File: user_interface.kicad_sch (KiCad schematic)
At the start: 0 parts

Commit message: feat: populate sensor and user interface schematic sheets; assign footprints
- Populated the Sensors schematic sheet with the following components:
    - BME280: Temperature and humidity sensor
    - Photoresistor: For measuring ambient light levels
    - Sound Sensor Section: Includes a microphone and preamplifier to amplify audio signals for microcontroller processing

- Populated the User Interface schematic sheet with:
    - Boot and reset controls for the microcontroller
    - Breakout lines for external devices:
        - One for I²C-based peripherals (e.g., OLED display)
        - One for general-purpose I/O devices

- Both the Sensors and User Interface sheets access necessary pins (e.g., I²C, GPIO, control signals) from the parent ESP32
sheet using hierarchical labels, enabling clean and modular design.

- Assigned appropriate footprints to all components.
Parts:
- added C19, C20: 0u1, Capacitor_SMD:C_0805_2012Metric, symbol Device:C
- added J4: Conn_01x04_Pin, Connector_PinHeader_2.54mm:PinHeader_1x04_P2.54mm_Vertical, symbol Connector:Conn_01x04_Pin
- added J5: Conn_01x05_Pin, Connector_PinHeader_2.54mm:PinHeader_1x05_P2.54mm_Vertical, symbol Connector:Conn_01x05_Pin
- added Q2, Q3: BC817, Package_TO_SOT_SMD:SOT-23, symbol Transistor_BJT:BC817
- added R30, R31, R32: 10k, Resistor_SMD:R_0805_2012Metric, symbol Device:R
- added S1: Boot, USLPT2819DT2TR:SW_USLPT2819DT2TR, symbol USLPT2819DT2TR:USLPT2819DT2TR
- added S2: Reset, USLPT2819DT2TR:SW_USLPT2819DT2TR, symbol USLPT2819DT2TR:USLPT2819DT2TR
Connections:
- new net: Q3.1 (B), R31.2
- new net: Q2.1 (B), R30.2
- new net +3.3V: J4.1 (Pin_1), J5.1 (Pin_1), R32.1
- new net BOOT: C19.2, Q2.2 (E), S1.3, S1.4
- new net DTR: Q2.3 (C), R31.1
- new net EN: C20.2, Q3.3 (C), R32.2, S2.3, S2.4
- new net GND: C19.1, C20.1, J4.4 (Pin_4), J5.5 (Pin_5), S1.1, S1.2, S2.1, S2.2
- new net GPIO18: J5.3 (Pin_3)
- new net GPIO19: J5.4 (Pin_4)
- new net GPIO8: J5.2 (Pin_2)
- new net RTS: Q3.2 (E), R30.1
- new net SCL: J4.3 (Pin_3)
- new net SDA: J4.2 (Pin_2)
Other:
- note added: "Breakout for remaining pins"
- note added: "OLED display connector (I2C)"
- note added: "Reset and BOOT Buttons"

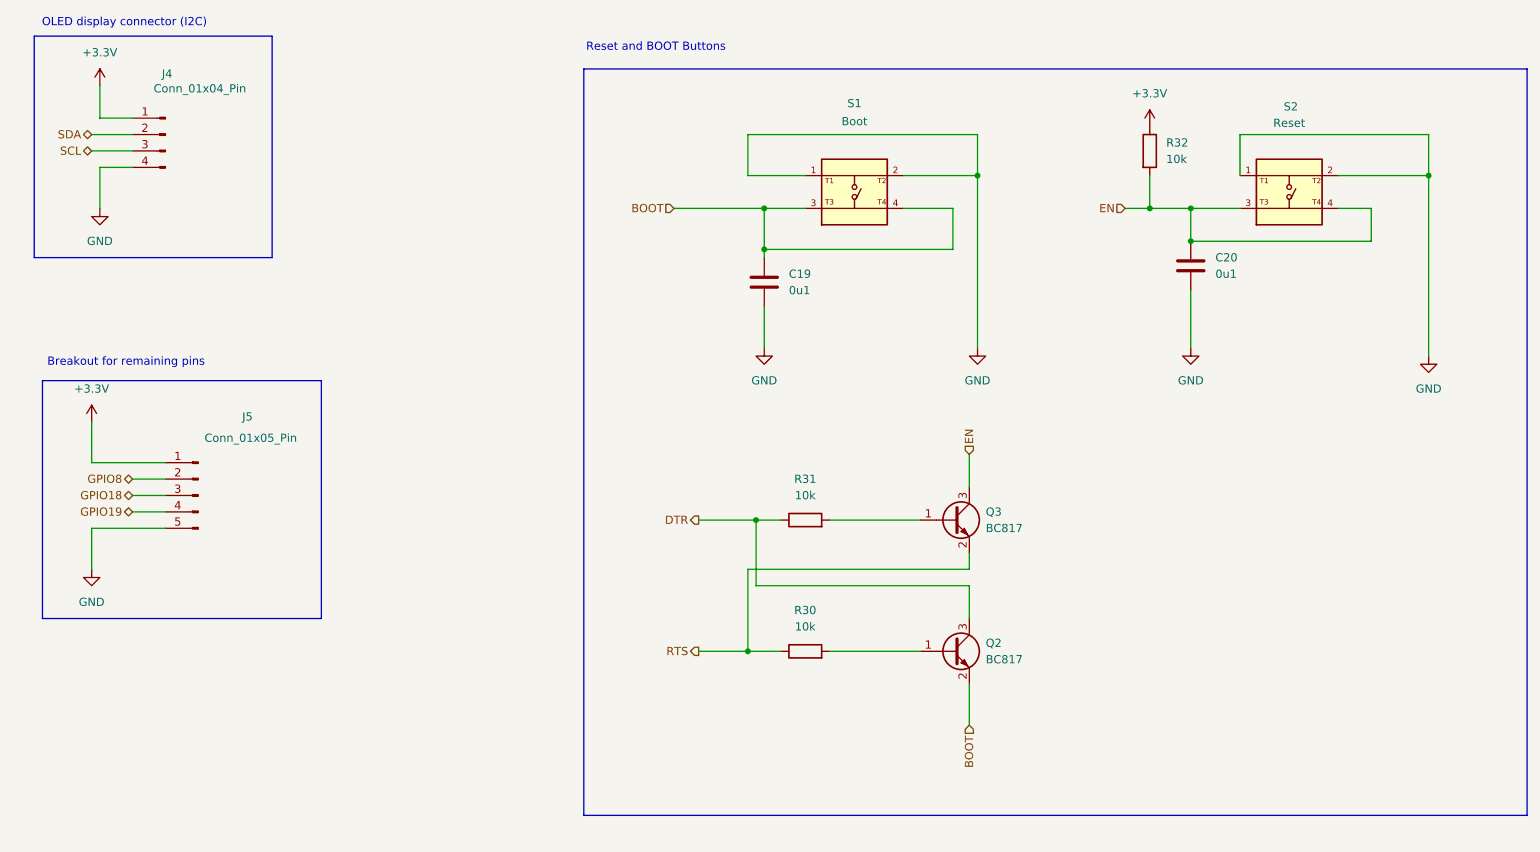
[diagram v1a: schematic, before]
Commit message: refactor: update label naming for net class scope resolution; set up PCB constraints
- Renamed schematic labels to follow a net class–based naming convention for
better scope resolution (e.g., labels in the SPI net class now use a SPI_ prefix).

- Configured the PCB stack-up to use a 4-layer board.

- Applied design constraints (e.g., trace width, spacing) based on the
PCB manufacturer's recommended specifications.
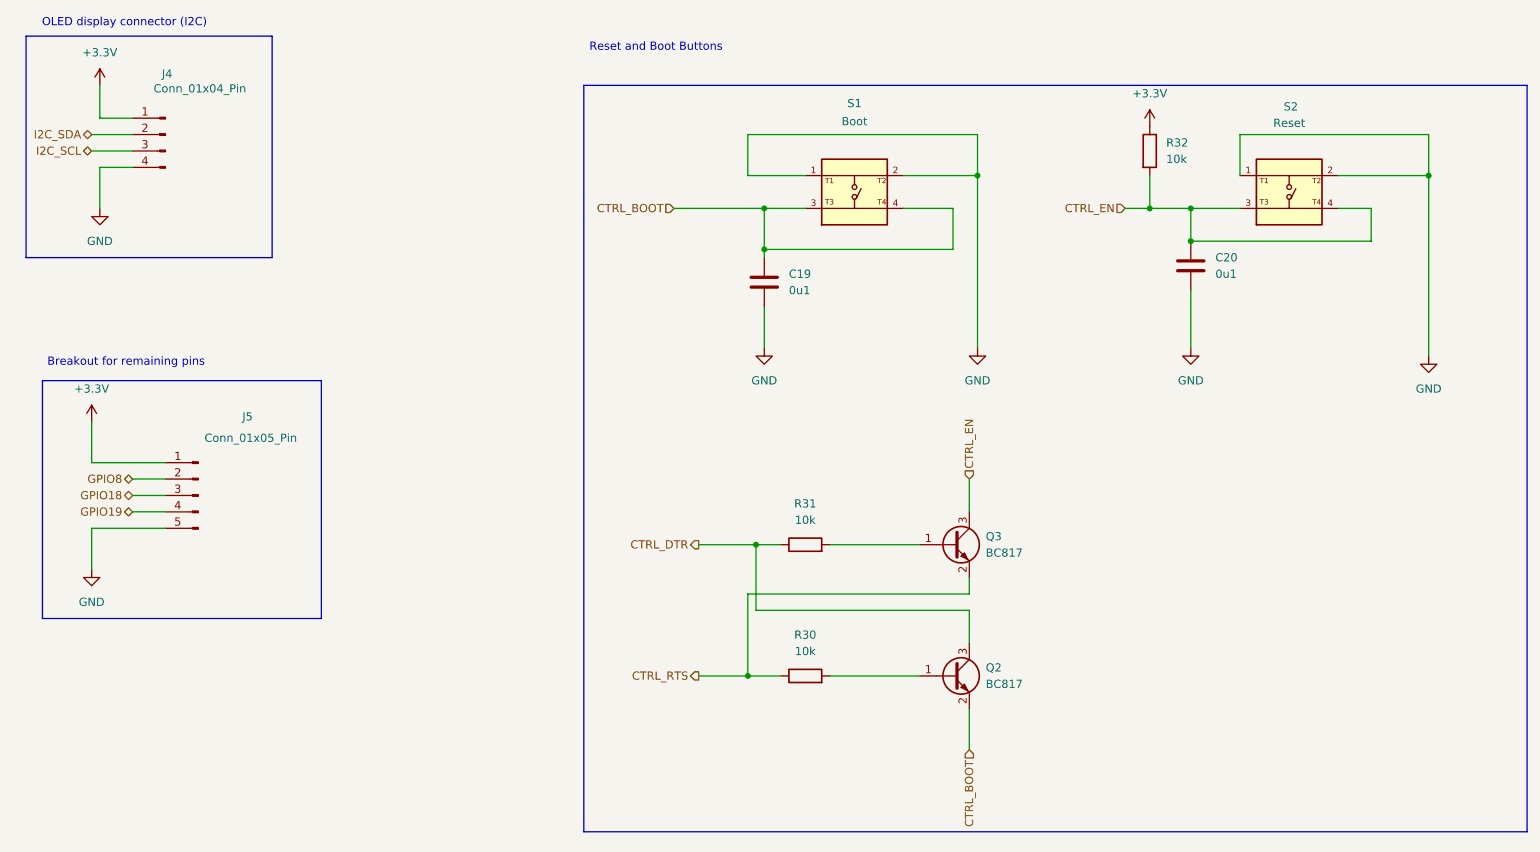
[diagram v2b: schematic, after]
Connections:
- net BOOT renamed CTRL_BOOT
- net DTR renamed CTRL_DTR
- net EN renamed CTRL_EN
- net RTS renamed CTRL_RTS
- net SCL renamed I2C_SCL
- net SDA renamed I2C_SDA
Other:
- note added: "Reset and Boot Buttons"
- note removed: "Reset and BOOT Buttons"
- moved on the sheet: Q2, Q3, R30, R31
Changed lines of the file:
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@@
 	)
 	(rectangle
-		(start 129.54 45.72)
-		(end 275.59 161.29)
+		(start 129.54 48.26)
+		(end 275.59 163.83)
 		(stroke
 			(width 0)
@@
 	)
 	(rectangle
-		(start 44.45 40.64)
+		(start 43.18 40.64)
 		(end 81.28 74.93)
 		(stroke
@@
 		)
 	)
-	(text "Reset and BOOT Buttons\n"
+	(text "Reset and Boot Buttons\n"
 		(exclude_from_sim no)
 		(at 140.716 42.418 0)
@@
 	)
 	(junction
-		(at 154.94 135.89)
+		(at 154.94 139.7)
 		(diameter 0)
 		(color 0 0 0 0)
@@
 	)
 	(junction
-		(at 156.21 115.57)
+		(at 156.21 119.38)
 		(diameter 0)
 		(color 0 0 0 0)
@@
 	(wire
 		(pts
-			(xy 154.94 123.19) (xy 154.94 135.89)
-		)
-		(stroke
-			(width 0)
-			(type default)
-		)
-	)
-	(wire
-		(pts
-			(xy 156.21 125.73) (xy 156.21 115.57)
-		)
-		(stroke
-			(width 0)
-			(type default)
-		)
-	)
-	(wire
-		(pts
-			(xy 189.23 120.65) (xy 189.23 123.19)
-		)
-		(stroke
-			(width 0)
-			(type default)
-		)
-	)
-	(wire
-		(pts
-			(xy 189.23 130.81) (xy 189.23 125.73)
+			(xy 154.94 127) (xy 154.94 139.7)
+		)
+		(stroke
+			(width 0)
+			(type default)
+		)
+	)
+	(wire
+		(pts
+			(xy 156.21 129.54) (xy 156.21 119.38)
+		)
+		(stroke
+			(width 0)
+			(type default)
+		)
+	)
+	(wire
+		(pts
+			(xy 189.23 124.46) (xy 189.23 127)
+		)
+		(stroke
+			(width 0)
+			(type default)
+		)
+	)
+	(wire
+		(pts
+			(xy 189.23 134.62) (xy 189.23 129.54)
 		)
 		(stroke
@@
 	(wire
 		(pts
-			(xy 189.23 123.19) (xy 154.94 123.19)
-		)
-		(stroke
-			(width 0)
-			(type default)
-		)
-	)
-	(wire
-		(pts
-			(xy 156.21 115.57) (xy 160.02 115.57)
+			(xy 189.23 127) (xy 154.94 127)
+		)
+		(stroke
+			(width 0)
+			(type default)
+		)
+	)
+	(wire
+		(pts
+			(xy 156.21 119.38) (xy 160.02 119.38)
 		)
 		(stroke
@@
 	(wire
 		(pts
-			(xy 189.23 140.97) (xy 189.23 147.32)
-		)
-		(stroke
-			(width 0)
-			(type default)
-		)
-	)
-	(wire
-		(pts
-			(xy 189.23 125.73) (xy 156.21 125.73)
-		)
-		(stroke
-			(width 0)
-			(type default)
-		)
-	)
-	(wire
-		(pts
-			(xy 154.94 135.89) (xy 160.02 135.89)
-		)
-		(stroke
-			(width 0)
-			(type default)
-		)
-	)
-	(wire
-		(pts
-			(xy 167.64 135.89) (xy 181.61 135.89)
+			(xy 189.23 144.78) (xy 189.23 151.13)
+		)
+		(stroke
+			(width 0)
+			(type default)
+		)
+	)
+	(wire
+		(pts
+			(xy 189.23 129.54) (xy 156.21 129.54)
+		)
+		(stroke
+			(width 0)
+			(type default)
+		)
+	)
+	(wire
+		(pts
+			(xy 154.94 139.7) (xy 160.02 139.7)
+		)
+		(stroke
+			(width 0)
+			(type default)
+		)
+	)
+	(wire
+		(pts
+			(xy 167.64 139.7) (xy 181.61 139.7)
 		)
 		(stroke
@@
 	(wire
 		(pts
-			(xy 189.23 105.41) (xy 189.23 110.49)
-		)
-		(stroke
-			(width 0)
-			(type default)
-		)
-	)
-	(wire
-		(pts
-			(xy 167.64 115.57) (xy 181.61 115.57)
+			(xy 189.23 109.22) (xy 189.23 114.3)
+		)
+		(stroke
+			(width 0)
+			(type default)
+		)
+	)
+	(wire
+		(pts
+			(xy 167.64 119.38) (xy 181.61 119.38)
 		)
 		(stroke
@@
 	(wire
 		(pts
-			(xy 147.32 135.89) (xy 154.94 135.89)
+			(xy 147.32 139.7) (xy 154.94 139.7)
 		)
 		(stroke
@@
 	(wire
 		(pts
-			(xy 147.32 115.57) (xy 156.21 115.57)
+			(xy 147.32 119.38) (xy 156.21 119.38)
 		)
 		(stroke
@@
 		)
 	)
-	(hierarchical_label "EN"
+	(hierarchical_label "CTRL_EN"
 		(shape input)
-		(at 189.23 105.41 90)
+		(at 189.23 109.22 90)
 		(effects
 			(font
@@
 		)
 	)
-	(hierarchical_label "SDA"
+	(hierarchical_label "I2C_SDA"
 		(shape bidirectional)
 		(at 53.34 55.88 180)
@@
 		)
 	)
-	(hierarchical_label "SCL"
+	(hierarchical_label "I2C_SCL"
 		(shape bidirectional)
 		(at 53.34 58.42 180)
@@
 		)
 	)
-	(hierarchical_label "EN"
+	(hierarchical_label "CTRL_EN"
 		(shape input)
 		(at 213.36 67.31 180)
@@
 		)
 	)
-	(hierarchical_label "DTR"
+	(hierarchical_label "CTRL_DTR"
 		(shape output)
-		(at 147.32 115.57 180)
+		(at 147.32 119.38 180)
 		(effects
 			(font
@@
 		)
 	)
-	(hierarchical_label "BOOT"
+	(hierarchical_label "CTRL_BOOT"
 		(shape input)
 		(at 143.51 67.31 180)
@@
 		)
 	)
-	(hierarchical_label "BOOT"
+	(hierarchical_label "CTRL_BOOT"
 		(shape input)
-		(at 189.23 147.32 270)
+		(at 189.23 151.13 270)
 		(effects
 			(font
@@
 		)
 	)
-	(hierarchical_label "RTS"
+	(hierarchical_label "CTRL_RTS"
 		(shape output)
-		(at 147.32 135.89 180)
+		(at 147.32 139.7 180)
 		(effects
 			(font
@@
 	(symbol
 		(lib_id "Device:R")
-		(at 163.83 115.57 90)
+		(at 163.83 119.38 90)
 		(unit 1)
 		(exclude_from_sim no)
@@
 		(fields_autoplaced yes)
 		(property "Reference" "R31"
-			(at 163.83 109.22 90)
+			(at 163.83 113.03 90)
 			(effects
 				(font
@@
 		)
 		(property "Value" "10k"
-			(at 163.83 111.76 90)
+			(at 163.83 115.57 90)
 			(effects
 				(font
@@
 		)
 		(property "Footprint" "Resistor_SMD:R_0805_2012Metric"
-			(at 163.83 117.348 90)
+			(at 163.83 121.158 90)
 			(effects
 				(font
@@
 		)
 		(property "Datasheet" "~"
-			(at 163.83 115.57 0)
+			(at 163.83 119.38 0)
 			(effects
 				(font
@@
 		)
 		(property "Description" "Resistor"
-			(at 163.83 115.57 0)
+			(at 163.83 119.38 0)
 			(effects
 				(font
@@
 	(symbol
 		(lib_id "Transistor_BJT:BC817")
-		(at 186.69 135.89 0)
+		(at 186.69 139.7 0)
 		(unit 1)
 		(exclude_from_sim no)
@@
 		(fields_autoplaced yes)
 		(property "Reference" "Q2"
-			(at 191.77 134.6199 0)
+			(at 191.77 138.4299 0)
 			(effects
 				(font
@@
 		)
 		(property "Value" "BC817"
-			(at 191.77 137.1599 0)
+			(at 191.77 140.9699 0)
 			(effects
 				(font
@@
 		)
 		(property "Footprint" "Package_TO_SOT_SMD:SOT-23"
-			(at 191.77 137.795 0)
+			(at 191.77 141.605 0)
 			(effects
 				(font
@@
 		)
 		(property "Datasheet" "https://www.onsemi.com/pub/Collateral/BC818-D.pdf"
-			(at 186.69 135.89 0)
+			(at 186.69 139.7 0)
 			(effects
 				(font
@@
 		)
 		(property "Description" "0.8A Ic, 45V Vce, NPN Transistor, SOT-23"
-			(at 186.69 135.89 0)
+			(at 186.69 139.7 0)
 			(effects
 				(font
@@
 	(symbol
 		(lib_id "Transistor_BJT:BC817")
-		(at 186.69 115.57 0)
+		(at 186.69 119.38 0)
 		(unit 1)
 		(exclude_from_sim no)
@@
 		(fields_autoplaced yes)
 		(property "Reference" "Q3"
-			(at 191.77 114.2999 0)
+			(at 191.77 118.1099 0)
 			(effects
 				(font
@@
 		)
 		(property "Value" "BC817"
-			(at 191.77 116.8399 0)
+			(at 191.77 120.6499 0)
 			(effects
 				(font
@@
 		)
 		(property "Footprint" "Package_TO_SOT_SMD:SOT-23"
-			(at 191.77 117.475 0)
+			(at 191.77 121.285 0)
 			(effects
 				(font
@@
 		)
 		(property "Datasheet" "https://www.onsemi.com/pub/Collateral/BC818-D.pdf"
-			(at 186.69 115.57 0)
+			(at 186.69 119.38 0)
 			(effects
 				(font
@@
 		)
 		(property "Description" "0.8A Ic, 45V Vce, NPN Transistor, SOT-23"
-			(at 186.69 115.57 0)
+			(at 186.69 119.38 0)
 			(effects
 				(font
@@
 	(symbol
 		(lib_id "Device:R")
-		(at 163.83 135.89 90)
+		(at 163.83 139.7 90)
 		(unit 1)
 		(exclude_from_sim no)
@@
 		(fields_autoplaced yes)
 		(property "Reference" "R30"
-			(at 163.83 129.54 90)
+			(at 163.83 133.35 90)
 			(effects
 				(font
@@
 		)
 		(property "Value" "10k"
-			(at 163.83 132.08 90)
+			(at 163.83 135.89 90)
 			(effects
 				(font
@@
 		)
 		(property "Footprint" "Resistor_SMD:R_0805_2012Metric"
-			(at 163.83 137.668 90)
+			(at 163.83 141.478 90)
 			(effects
 				(font
@@
 		)
 		(property "Datasheet" "~"
-			(at 163.83 135.89 0)
+			(at 163.83 139.7 0)
 			(effects
 				(font
@@
 		)
 		(property "Description" "Resistor"
-			(at 163.83 135.89 0)
-			(effects
-				(font
+			(at 163.83 139.7 0)
+			(effects
+				(font
